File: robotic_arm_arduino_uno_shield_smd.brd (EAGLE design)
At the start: 44.5 x 53.3 mm, 39 parts, among them J1 (ID,OD)=(2.1,5.5)MM

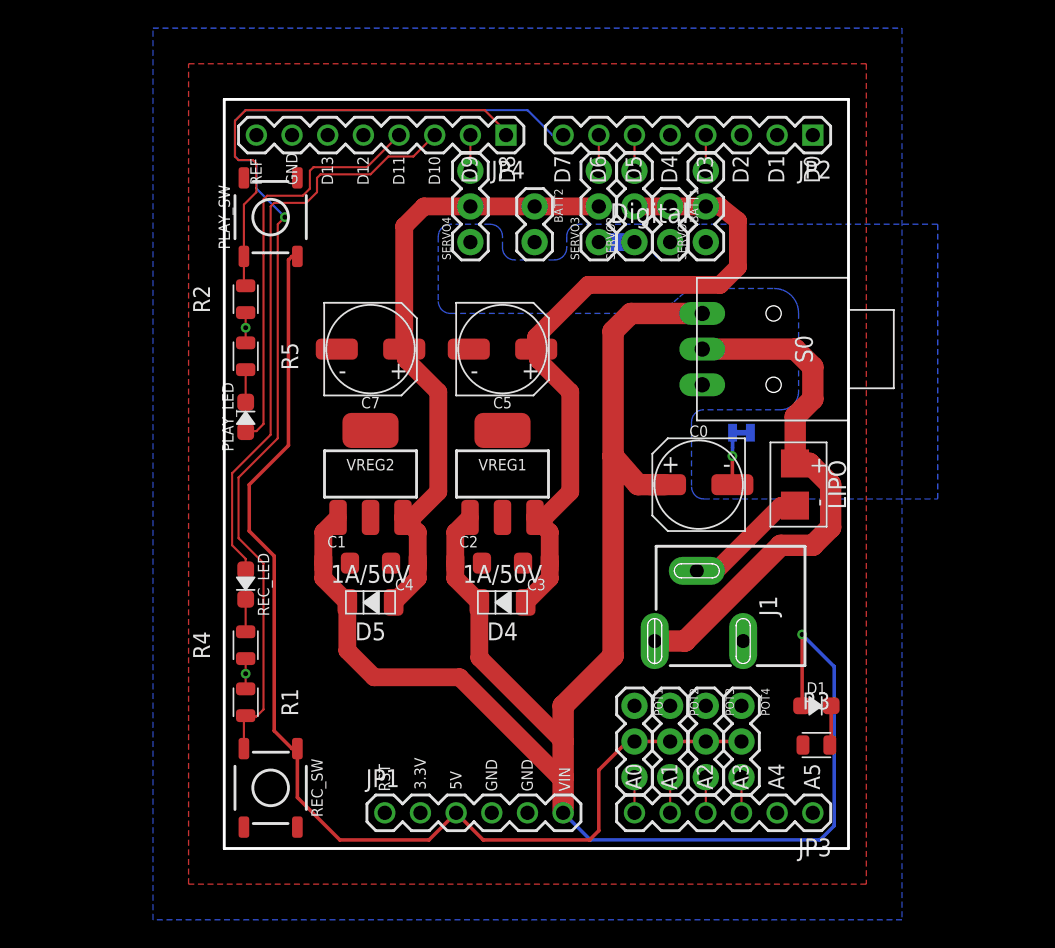
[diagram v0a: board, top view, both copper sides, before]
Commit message: Adjusted some of the traces
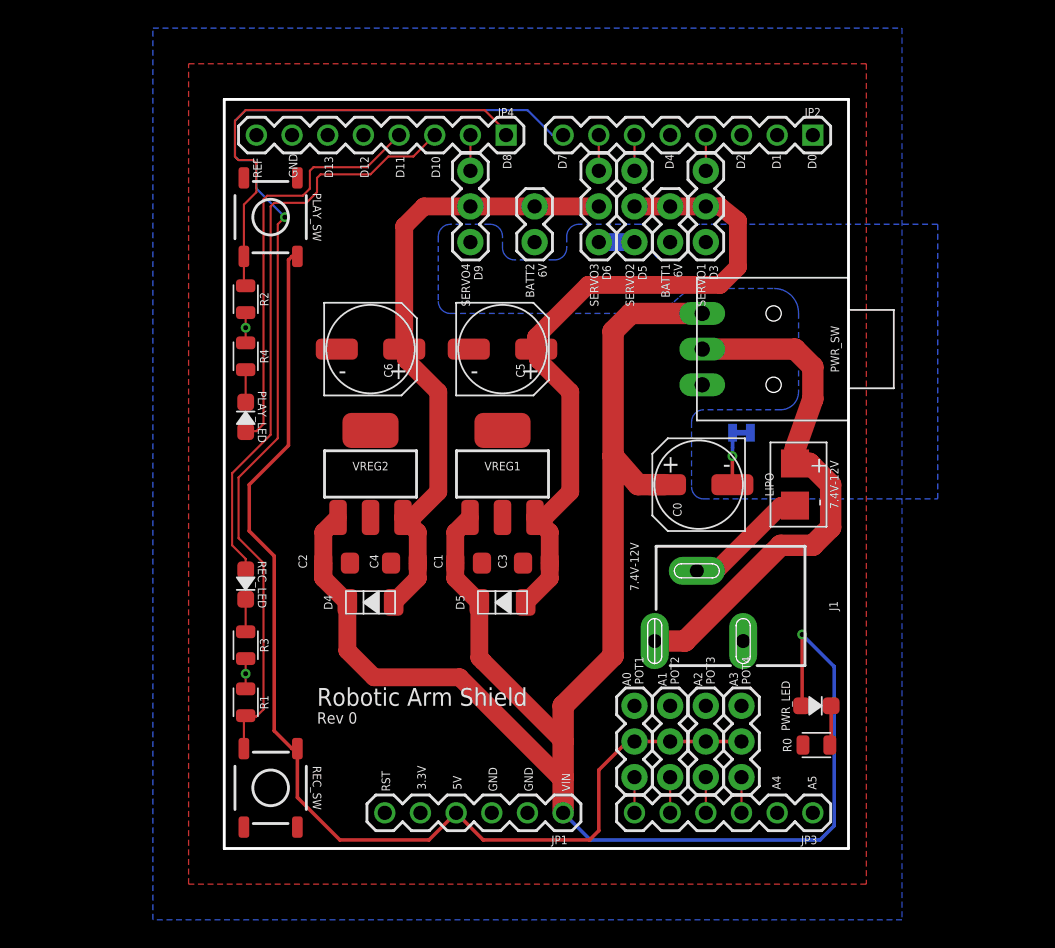
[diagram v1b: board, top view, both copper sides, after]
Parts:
- removed R5: 10KΩ, MrSwirlyEyes:RESC2012X60_HS
- added R0: 10KΩ, MrSwirlyEyes:RESC2012X60_HS
- BATT1, BATT2: value (none) -> 6V
- POT1, POT2, POT3, POT4: value (none) -> 22K
- moved R3 41.3 mm to (1.52, 14.5), turned to 90 degrees
- moved R4 20.6 mm to (1.52, 35.1), turned to 270 degrees
- moved C1 9.40 mm to (17.4, 20.3)
- moved C2 9.40 mm to (8.00, 20.3)
- moved D4 9.40 mm to (10.4, 17.5)
- moved D5 9.40 mm to (19.8, 17.5)
- renumbered C7 to C6, D1 to PWR_LED, S0 to PWR_SW
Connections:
- net GND: now also R0.1; no longer R5.1
- net N$1: now also R4.2; no longer R5.2
- net N$2: now also R3.2; no longer R4.2
- net N$4: now also R0.2; no longer R3.2
- net VCC_1: now also D5.A; no longer D4.A
- net VCC_2: now also D4.A; no longer D5.A
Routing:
- net VIN: track 136.7 -> 137.8 mm
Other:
- board text added: "1A/50V"
- board text added: "6V"
- board text added: "7.4V-12V"
- board text added: "CADed by: MrSwirlyEyes"
- board text added: "Designed by: Buu Truong"
- board text added: "Rev 0"
- board text added: "Robotic Arm Shield"
- board text removed: "Digital"

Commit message: Final version.  Sending to fab
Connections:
- net N$3 renamed VBATT
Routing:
- net VIN: track 137.8 -> 62.4 mm
- net VBATT: track 37.6 -> 0.00 mm
- net 5V: track 81.7 -> 80.0 mm
- net D7: track 74.4 -> 72.9 mm
- net D10: track 41.8 -> 41.0 mm
- net VCC_1: track 49.9 -> 49.2 mm
- net D8: track 33.9 -> 34.6 mm
- added copper zone on layer 1, net VBATT
- added copper zone on layer 1, net VIN

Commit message: Changed out switch.  Adjusted traces accordingly
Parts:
- removed PWR_SW: SPDT, MrSwirlyEyes:SW_SPDT_RA_5A/28V/120VAC
- added S1: (no value), SparkFun-Switches:SWITCH_SPDT_PTH_11.6X4.0MM
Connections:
- net VBATT: now also S1.2; no longer PWR_SW.2
- net VIN: now also S1.1; no longer PWR_SW.3
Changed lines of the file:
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@@
 <attribute name="NAME" x="38.814" y="25.916" size="0.6096" layer="25" font="vector" ratio="10" rot="R270" align="center"/>
-</element>
-<element name="PWR_SW" library="MrSwirlyEyes" package="SW_SPDT_RA_5A/28V/120VAC" value="SPDT" x="36.576" y="35.56" smashed="yes" rot="R90">
-<attribute name="CREATOR" value="MrSwirlyEyes" x="36.576" y="35.56" size="1.778" layer="27" rot="R90" display="off"/>
-<attribute name="DATASHEET" value="http://spec_sheets.e-switch.com/specs/T551101.pdf" x="36.576" y="35.56" size="1.778" layer="27" rot="R90" display="off"/>
-<attribute name="DIST" value="Digikey" x="36.576" y="35.56" size="1.778" layer="27" rot="R90" display="off"/>
-<attribute name="DISTLINK" value="https://www.digikey.com/products/en?keywords=EG2483-ND" x="36.576" y="35.56" size="1.778" layer="27" rot="R90" display="off"/>
-<attribute name="DISTPN" value="EG2483-ND" x="36.576" y="35.56" size="1.778" layer="27" rot="R90" display="off"/>
-<attribute name="MFR" value="E-Switch" x="36.576" y="35.56" size="1.778" layer="27" rot="R90" display="off"/>
-<attribute name="MPN" value="500ASSP1M6QE" x="36.576" y="35.56" size="1.778" layer="27" rot="R90" display="off"/>
-<attribute name="NAME" x="43.18" y="35.56" size="0.6096" layer="25" font="vector" ratio="10" rot="R90" align="top-center"/>
-<attribute name="TESTED" value="NO" x="36.576" y="35.56" size="1.778" layer="27" rot="R90" display="off"/>
 </element>
 <element name="VREG1" library="MrSwirlyEyes" package="SOT223" value="1.5A/5V" x="19.812" y="26.67" smashed="yes">
@@
 </element>
 <element name="SUPPLY14" library="SparkFun-PowerSymbols" package="2PT_GND_TIE" value="2PT_GND_TIE" x="36.83" y="29.604" smashed="yes" rot="MR90"/>
+<element name="S1" library="SparkFun-Switches" package="SWITCH_SPDT_PTH_11.6X4.0MM" value="" x="42.164" y="35.56">
+<attribute name="PROD_ID" value="SWCH-08261" x="42.164" y="35.56" size="0.6096" layer="27" ratio="10" display="off"/>
+<attribute name="SF_SKU" value="COM-00102" x="42.164" y="35.56" size="0.6096" layer="27" ratio="10" display="off"/>
+</element>
 </elements>
 <signals>
@@
 <contactref element="JP1" pad="6"/>
 <contactref element="PWR_LED" pad="A"/>
-<contactref element="PWR_SW" pad="3"/>
 <contactref element="VREG1" pad="1"/>
 <contactref element="VREG2" pad="1"/>
@@
 <wire x1="16.449" y1="19.239" x2="18.162" y2="17.526" width="1.143" layer="1"/>
 <polygon width="0.254" layer="1" isolate="0.254">
-<vertex x="34.798" y="37.592"/>
-<vertex x="31.496" y="37.592"/>
-<vertex x="30.48" y="36.576"/>
-<vertex x="30.48" y="30.226"/>
-<vertex x="33.02" y="27.94"/>
-<vertex x="33.02" y="24.384"/>
+<vertex x="43.434" y="37.592"/>
+<vertex x="39.37" y="37.592"/>
+<vertex x="31.496" y="29.718"/>
+<vertex x="31.496" y="24.384"/>
 <vertex x="24.638" y="16.764"/>
 <vertex x="24.638" y="2.286"/>
@@
 <vertex x="24.13" y="18.796"/>
 <vertex x="24.13" y="36.576"/>
-<vertex x="26.67" y="38.862"/>
-<vertex x="34.798" y="38.862"/>
+<vertex x="26.416" y="38.608"/>
+<vertex x="43.434" y="38.608"/>
 </polygon>
 <wire x1="8.636" y1="17.526" x2="8.764" y2="17.526" width="1.27" layer="1"/>
@@
 <wire x1="8.764" y1="17.526" x2="7.051" y2="19.239" width="1.143" layer="1"/>
 <wire x1="7.051" y1="19.239" x2="7.051" y2="20.32" width="1.143" layer="1"/>
+<contactref element="S1" pad="1"/>
 </signal>
 <signal name="5V">
@@
 <signal name="VBATT">
 <contactref element="LIPO" pad="V+"/>
-<contactref element="PWR_SW" pad="2"/>
 <contactref element="J1" pad="PWR"/>
 <polygon width="0.254" layer="1">
-<vertex x="48.26" y="36.83"/>
-<vertex x="31.75" y="36.83"/>
-<vertex x="31.242" y="36.322"/>
-<vertex x="31.242" y="30.48"/>
-<vertex x="39.116" y="30.48"/>
-<vertex x="39.624" y="29.972"/>
+<vertex x="53.34" y="36.83"/>
+<vertex x="39.624" y="36.83"/>
+<vertex x="35.56" y="33.02"/>
+<vertex x="35.56" y="32.766"/>
+<vertex x="39.624" y="28.702"/>
 <vertex x="39.624" y="25.908"/>
 <vertex x="42.164" y="25.908"/>
@@
 <vertex x="33.274" y="14.478"/>
 <vertex x="36.322" y="17.272"/>
-<vertex x="48.26" y="17.272"/>
+<vertex x="53.34" y="17.272"/>
 </polygon>
+<contactref element="S1" pad="2"/>
 </signal>
 <signal name="N$1">
@@
 <wire x1="29.21" y1="43.18" x2="26.67" y2="43.18" width="1.27" layer="16"/>
 <polygon width="0.254" layer="16" isolate="0.254">
-<vertex x="40.894" y="39.878"/>
-<vertex x="40.894" y="31.242"/>
-<vertex x="33.274" y="31.242"/>
-<vertex x="33.274" y="24.892"/>
-<vertex x="50.8" y="24.892"/>
+<vertex x="17.018" y="38.1"/>
+<vertex x="31.496" y="38.1"/>
+<vertex x="34.29" y="35.56"/>
+<vertex x="34.29" y="24.638"/>
+<vertex x="50.8" y="24.638"/>
 <vertex x="50.8" y="44.196"/>
 <vertex x="33.02" y="44.196"/>
@@
 <vertex x="30.48" y="41.91"/>
 <vertex x="30.48" y="44.196"/>
-<vertex x="24.638" y="44.196"/>
-<vertex x="24.638" y="41.148"/>
-<vertex x="19.558" y="41.148"/>
-<vertex x="19.558" y="44.196"/>
-<vertex x="15.494" y="44.196"/>
-<vertex x="15.494" y="38.1"/>
-<vertex x="29.585615625" y="38.1" curve="45"/>
-<vertex x="32.413240625" y="39.271240625" curve="-45"/>
-<vertex x="33.8780875" y="39.878"/>
+<vertex x="25.146" y="44.196"/>
+<vertex x="24.638" y="43.688"/>
+<vertex x="24.638" y="41.91"/>
+<vertex x="23.876" y="41.148"/>
+<vertex x="20.32" y="41.148"/>
+<vertex x="19.558" y="41.91"/>
+<vertex x="19.558" y="43.688"/>
+<vertex x="19.05" y="44.196"/>
+<vertex x="16.256" y="44.196"/>
+<vertex x="15.494" y="43.434"/>
+<vertex x="15.494" y="39.624"/>
 </polygon>
 <contactref element="SUPPLY14" pad="P$1"/>

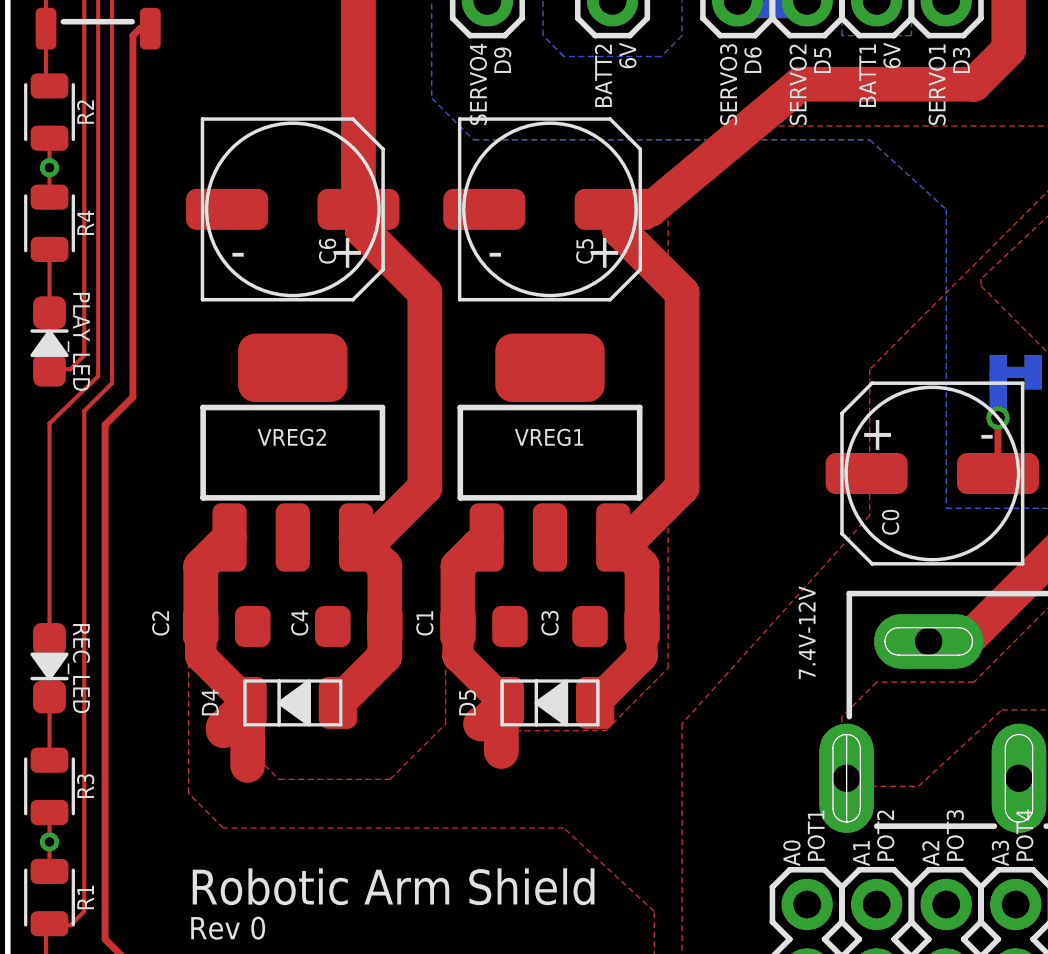
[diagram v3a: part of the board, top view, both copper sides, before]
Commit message: Small adjusted traces before fab
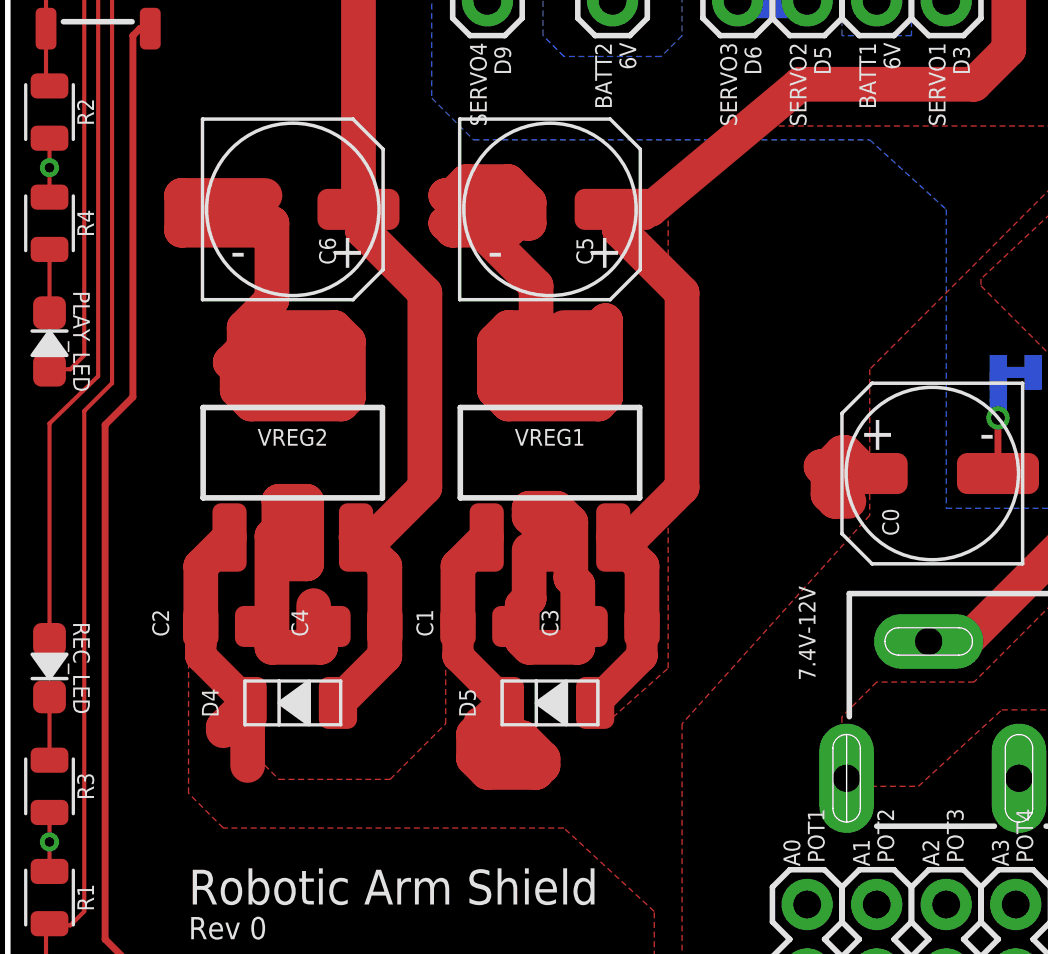
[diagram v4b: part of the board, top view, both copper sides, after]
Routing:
- net GND: track 8.00 -> 91.0 mm
- net VIN: track 62.4 -> 73.5 mm
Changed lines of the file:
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@@
 <contactref element="C2" pad="2"/>
 <contactref element="C1" pad="2"/>
+<wire x1="17.412" y1="35.56" x2="16.904" y2="35.052" width="1.27" layer="1"/>
+<wire x1="16.904" y1="35.052" x2="16.002" y2="35.052" width="1.27" layer="1"/>
+<wire x1="16.002" y1="35.052" x2="16.256" y2="34.798" width="1.27" layer="1"/>
+<wire x1="16.256" y1="34.798" x2="18.288" y2="34.798" width="1.27" layer="1"/>
+<wire x1="18.288" y1="34.798" x2="18.542" y2="35.052" width="1.27" layer="1"/>
+<wire x1="18.542" y1="35.052" x2="19.05" y2="35.052" width="1.27" layer="1"/>
+<wire x1="19.05" y1="35.052" x2="19.05" y2="35.814" width="1.27" layer="1"/>
+<wire x1="19.05" y1="35.814" x2="18.288" y2="36.576" width="1.27" layer="1"/>
+<wire x1="16.764" y1="36.576" x2="16.256" y2="36.068" width="1.27" layer="1"/>
+<wire x1="16.256" y1="36.068" x2="16.002" y2="36.068" width="1.27" layer="1"/>
+<wire x1="16.002" y1="36.068" x2="19.304" y2="32.766" width="1.27" layer="1"/>
+<wire x1="19.304" y1="32.766" x2="19.304" y2="31.242" width="1.27" layer="1"/>
+<wire x1="19.304" y1="31.242" x2="18.288" y2="31.242" width="1.27" layer="1"/>
+<wire x1="18.288" y1="31.242" x2="17.78" y2="30.734" width="1.27" layer="1"/>
+<wire x1="17.78" y1="30.734" x2="17.78" y2="28.956" width="1.27" layer="1"/>
+<wire x1="17.78" y1="28.956" x2="18.288" y2="28.448" width="1.27" layer="1"/>
+<wire x1="18.288" y1="28.448" x2="21.59" y2="28.448" width="1.27" layer="1"/>
+<wire x1="21.59" y1="28.448" x2="21.844" y2="28.702" width="1.27" layer="1"/>
+<wire x1="21.844" y1="28.702" x2="21.844" y2="31.496" width="1.27" layer="1"/>
+<wire x1="21.844" y1="31.496" x2="21.59" y2="31.242" width="1.27" layer="1"/>
+<wire x1="21.59" y1="31.242" x2="20.32" y2="31.242" width="1.27" layer="1"/>
+<wire x1="18.288" y1="36.576" x2="16.764" y2="36.576" width="1.27" layer="1"/>
+<wire x1="10.414" y1="29.769" x2="10.109" y2="29.464" width="1.27" layer="1"/>
+<wire x1="10.109" y1="29.464" x2="8.382" y2="29.464" width="1.27" layer="1"/>
+<wire x1="8.382" y1="29.464" x2="8.382" y2="28.956" width="1.27" layer="1"/>
+<wire x1="8.382" y1="28.956" x2="8.89" y2="28.448" width="1.27" layer="1"/>
+<wire x1="8.89" y1="28.448" x2="12.192" y2="28.448" width="1.27" layer="1"/>
+<wire x1="12.192" y1="28.448" x2="12.446" y2="28.702" width="1.27" layer="1"/>
+<wire x1="12.446" y1="28.702" x2="12.446" y2="30.734" width="1.27" layer="1"/>
+<wire x1="12.446" y1="30.734" x2="11.938" y2="31.242" width="1.27" layer="1"/>
+<wire x1="11.938" y1="31.242" x2="9.652" y2="31.242" width="1.27" layer="1"/>
+<wire x1="9.652" y1="31.242" x2="8.382" y2="29.972" width="1.27" layer="1"/>
+<wire x1="8.382" y1="29.972" x2="8.128" y2="29.972" width="1.27" layer="1"/>
+<wire x1="8.128" y1="29.972" x2="8.636" y2="30.48" width="1.27" layer="1"/>
+<wire x1="8.636" y1="30.48" x2="8.636" y2="31.242" width="1.27" layer="1"/>
+<wire x1="8.636" y1="31.242" x2="9.652" y2="32.258" width="1.27" layer="1"/>
+<wire x1="9.652" y1="32.258" x2="9.652" y2="35.052" width="1.27" layer="1"/>
+<wire x1="9.652" y1="35.052" x2="9.398" y2="34.798" width="1.27" layer="1"/>
+<wire x1="9.398" y1="34.798" x2="6.35" y2="34.798" width="1.27" layer="1"/>
+<wire x1="6.35" y1="34.798" x2="6.35" y2="36.068" width="1.27" layer="1"/>
+<wire x1="6.35" y1="36.068" x2="9.398" y2="36.068" width="1.27" layer="1"/>
+<wire x1="10.414" y1="23.5712" x2="9.906" y2="23.0632" width="1.27" layer="1"/>
+<wire x1="9.906" y1="23.0632" x2="9.906" y2="22.606" width="1.27" layer="1"/>
+<wire x1="9.906" y1="22.606" x2="10.922" y2="22.606" width="1.27" layer="1"/>
+<wire x1="10.922" y1="22.606" x2="10.922" y2="24.892" width="1.27" layer="1"/>
+<wire x1="10.922" y1="24.892" x2="9.906" y2="24.892" width="1.27" layer="1"/>
+<wire x1="9.906" y1="24.892" x2="9.906" y2="23.876" width="1.27" layer="1"/>
+<wire x1="9.906" y1="23.876" x2="9.652" y2="23.622" width="1.27" layer="1"/>
+<wire x1="9.652" y1="19.558" x2="11.43" y2="19.558" width="1.27" layer="1"/>
+<wire x1="11.43" y1="19.558" x2="11.176" y2="19.812" width="1.27" layer="1"/>
+<wire x1="11.176" y1="19.812" x2="11.176" y2="21.082" width="1.27" layer="1"/>
+<wire x1="9.652" y1="23.622" x2="9.652" y2="19.558" width="1.27" layer="1"/>
+<wire x1="19.812" y1="23.5712" x2="19.05" y2="24.3332" width="1.27" layer="1"/>
+<wire x1="19.05" y1="24.3332" x2="19.05" y2="24.638" width="1.27" layer="1"/>
+<wire x1="19.05" y1="24.638" x2="20.066" y2="24.638" width="1.27" layer="1"/>
+<wire x1="20.066" y1="24.638" x2="20.574" y2="24.13" width="1.27" layer="1"/>
+<wire x1="20.574" y1="24.13" x2="20.574" y2="22.098" width="1.27" layer="1"/>
+<wire x1="20.574" y1="22.098" x2="20.828" y2="21.844" width="1.27" layer="1"/>
+<wire x1="20.828" y1="19.558" x2="19.05" y2="19.558" width="1.27" layer="1"/>
+<wire x1="19.05" y1="19.558" x2="18.796" y2="19.812" width="1.27" layer="1"/>
+<wire x1="18.796" y1="19.812" x2="18.796" y2="21.082" width="1.27" layer="1"/>
+<wire x1="18.796" y1="21.082" x2="19.05" y2="21.336" width="1.27" layer="1"/>
+<wire x1="19.05" y1="21.336" x2="19.05" y2="23.114" width="1.27" layer="1"/>
+<wire x1="20.828" y1="21.844" x2="20.828" y2="19.558" width="1.27" layer="1"/>
 </signal>
 <signal name="AREF">
@@
 <vertex x="16.002" y="19.05"/>
 <vertex x="18.542" y="16.764"/>
-<vertex x="18.542" y="16.51"/>
-<vertex x="21.844" y="16.51"/>
+<vertex x="21.844" y="16.764"/>
 <vertex x="24.13" y="18.796"/>
 <vertex x="24.13" y="36.576"/>
@@
 <wire x1="7.051" y1="19.239" x2="7.051" y2="20.32" width="1.143" layer="1"/>
 <contactref element="S1" pad="1"/>
+<wire x1="18.162" y1="17.526" x2="17.018" y2="16.382" width="1.27" layer="1"/>
+<wire x1="17.018" y1="16.382" x2="17.018" y2="15.494" width="1.27" layer="1"/>
+<wire x1="17.018" y1="15.494" x2="17.526" y2="14.986" width="1.27" layer="1"/>
+<wire x1="17.526" y1="14.986" x2="19.304" y2="14.986" width="1.27" layer="1"/>
+<wire x1="19.304" y1="14.986" x2="19.558" y2="15.24" width="1.27" layer="1"/>
+<wire x1="19.558" y1="15.24" x2="19.558" y2="15.494" width="1.27" layer="1"/>
+<wire x1="19.558" y1="15.494" x2="18.796" y2="16.256" width="1.27" layer="1"/>
+<wire x1="18.796" y1="16.256" x2="18.542" y2="16.256" width="1.27" layer="1"/>
+<wire x1="31.382" y1="25.908" x2="30.62" y2="26.67" width="1.27" layer="1"/>
+<wire x1="30.62" y1="26.67" x2="30.48" y2="26.67" width="1.27" layer="1"/>
+<wire x1="30.48" y1="26.67" x2="29.972" y2="26.162" width="1.27" layer="1"/>
+<wire x1="29.972" y1="26.162" x2="29.718" y2="26.162" width="1.27" layer="1"/>
+<wire x1="29.718" y1="26.162" x2="29.972" y2="25.908" width="1.27" layer="1"/>
+<wire x1="29.972" y1="25.908" x2="29.972" y2="25.146" width="1.27" layer="1"/>
+<wire x1="29.972" y1="25.146" x2="30.226" y2="24.892" width="1.27" layer="1"/>
+<wire x1="30.226" y1="24.892" x2="30.734" y2="24.892" width="1.27" layer="1"/>
 </signal>
 <signal name="5V">
